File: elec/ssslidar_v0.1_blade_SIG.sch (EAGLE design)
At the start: 30 parts, among them P1 PIN_SMD_0.8X1_RECT, P10 PIN_SMD_0.8X1_RECT, P11 PIN_SMD_1X1_RECT, P12 PIN_SMD_0.8X1_RECT, P13 PIN_SMD_0.8X1_RECT, P14 PIN_SMD_0.8X1_RECT, P15 PIN_SMD_0.8X1_RECT, P16 PIN_SMD_0.8X1_RECT, P17 PIN_SMD_1X1_RECT, P18 PIN_SMD_0.8X1_RECT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

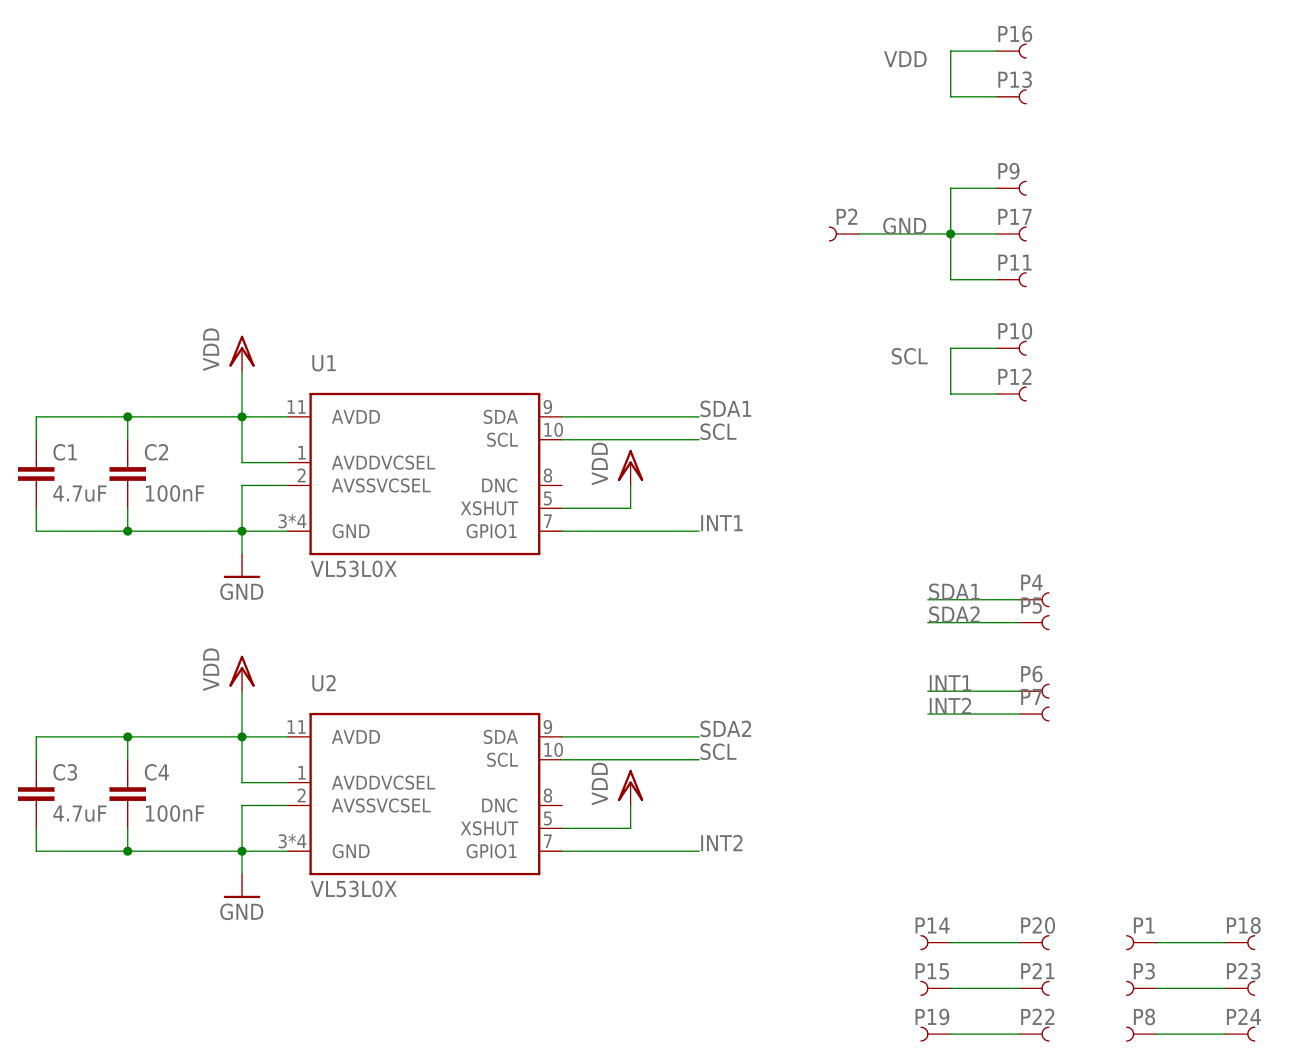
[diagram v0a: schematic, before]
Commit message: Working on main board Made blades longer to avoid too much occlusion from the main PCB (but we will still need to put the whole thing on a mast).
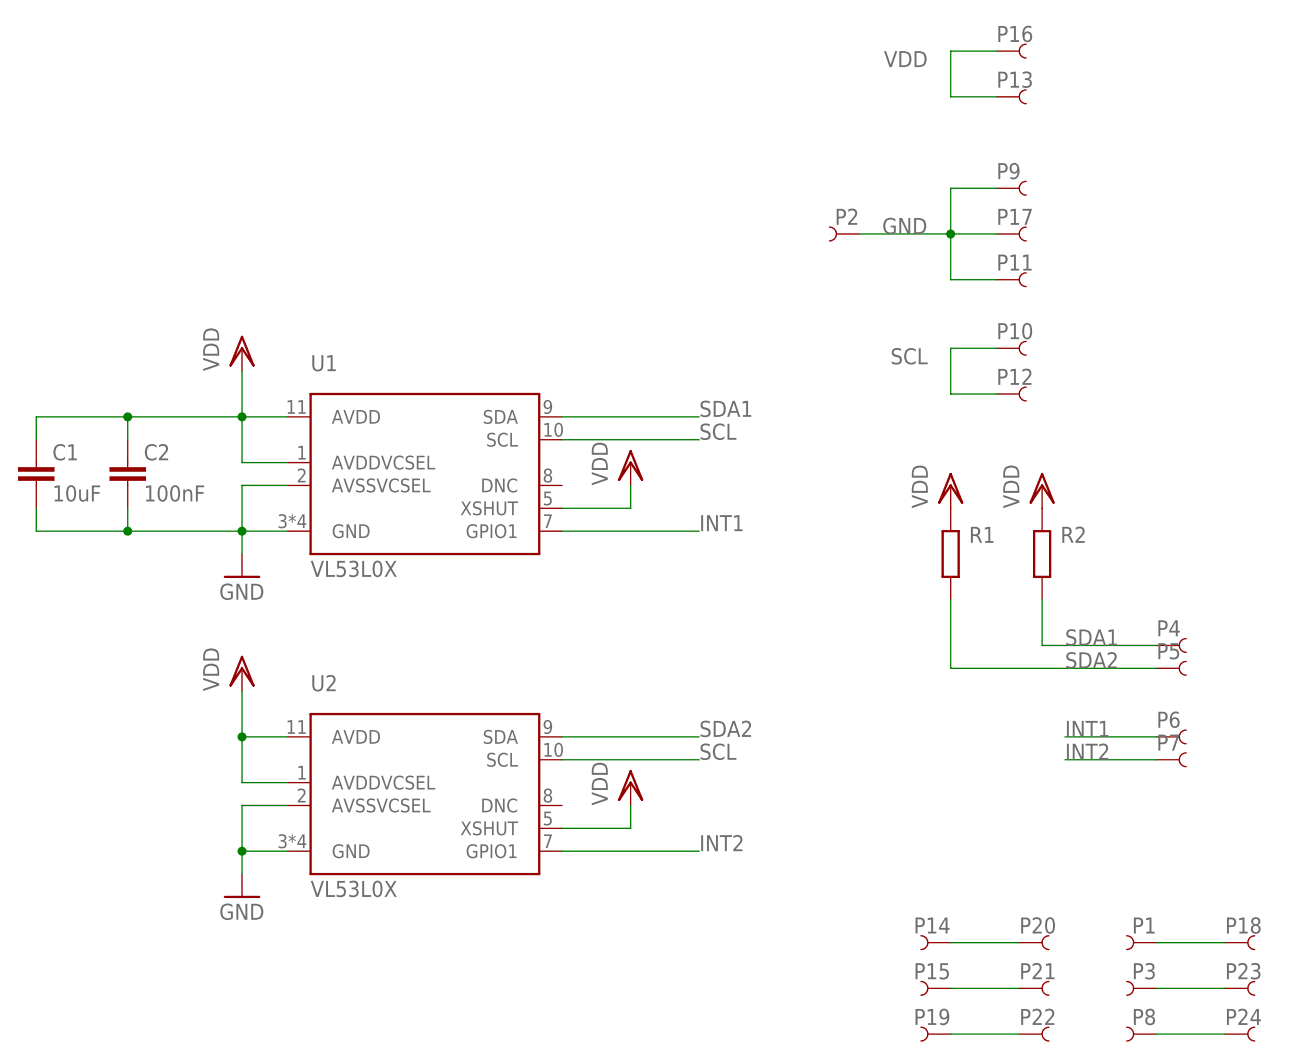
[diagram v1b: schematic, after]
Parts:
- removed C3: 4.7uF, Xevelabs:C0603
- removed C4: 100nF, Xevelabs:C0201
- added R1, R2: (no value), Xevelabs:R0402
- C1: value 4.7uF -> 10uF; device Xevelabs:C0603 -> Xevelabs:C0805
- C2: device Xevelabs:C0201 -> Xevelabs:C0402
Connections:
- net GND: no longer C3.2, C4.2
- net SDA1: now also R2.1
- net SDA2: now also R1.1
- net VDD: now also R1.2, R2.2; no longer C3.1, C4.1
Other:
- moved on the sheet: P4, P5, P6, P7

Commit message: Updated blades (ready for release). Double power rail for sensors.
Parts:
- added C3: 100nF, Xevelabs:C0402
- R1, R2: value (none) -> 2k
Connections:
- net GND: now also C3.2
- net VDD: now also C3.1
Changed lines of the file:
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@@
 <grid distance="0.1" unitdist="inch" unit="inch" style="lines" multiple="1" display="no" altdistance="0.01" altunitdist="inch" altunit="inch"/>
 <layers>
-<layer number="1" name="Top" color="4" fill="1" visible="yes" active="no"/>
-<layer number="2" name="Route2" color="1" fill="3" visible="yes" active="no"/>
-<layer number="3" name="Route3" color="4" fill="3" visible="yes" active="no"/>
-<layer number="14" name="Route14" color="1" fill="6" visible="yes" active="no"/>
-<layer number="15" name="Route15" color="4" fill="6" visible="yes" active="no"/>
-<layer number="16" name="Bottom" color="1" fill="1" visible="yes" active="no"/>
-<layer number="17" name="Pads" color="2" fill="1" visible="yes" active="no"/>
-<layer number="18" name="Vias" color="2" fill="1" visible="yes" active="no"/>
-<layer number="19" name="Unrouted" color="6" fill="1" visible="yes" active="no"/>
-<layer number="20" name="Dimension" color="15" fill="1" visible="yes" active="no"/>
-<layer number="21" name="tPlace" color="7" fill="1" visible="yes" active="no"/>
-<layer number="22" name="bPlace" color="7" fill="1" visible="yes" active="no"/>
-<layer number="23" name="tOrigins" color="15" fill="1" visible="yes" active="no"/>
-<layer number="24" name="bOrigins" color="15" fill="1" visible="yes" active="no"/>
-<layer number="25" name="tNames" color="7" fill="1" visible="yes" active="no"/>
-<layer number="26" name="bNames" color="7" fill="1" visible="yes" active="no"/>
-<layer number="27" name="tValues" color="7" fill="1" visible="yes" active="no"/>
-<layer number="28" name="bValues" color="7" fill="1" visible="yes" active="no"/>
+<layer number="1" name="Top" color="4" fill="1" visible="no" active="no"/>
+<layer number="2" name="Route2" color="1" fill="3" visible="no" active="no"/>
+<layer number="3" name="Route3" color="4" fill="3" visible="no" active="no"/>
+<layer number="14" name="Route14" color="1" fill="6" visible="no" active="no"/>
+<layer number="15" name="Route15" color="4" fill="6" visible="no" active="no"/>
+<layer number="16" name="Bottom" color="1" fill="1" visible="no" active="no"/>
+<layer number="17" name="Pads" color="2" fill="1" visible="no" active="no"/>
+<layer number="18" name="Vias" color="2" fill="1" visible="no" active="no"/>
+<layer number="19" name="Unrouted" color="6" fill="1" visible="no" active="no"/>
+<layer number="20" name="Dimension" color="15" fill="1" visible="no" active="no"/>
+<layer number="21" name="tPlace" color="7" fill="1" visible="no" active="no"/>
+<layer number="22" name="bPlace" color="7" fill="1" visible="no" active="no"/>
+<layer number="23" name="tOrigins" color="15" fill="1" visible="no" active="no"/>
+<layer number="24" name="bOrigins" color="15" fill="1" visible="no" active="no"/>
+<layer number="25" name="tNames" color="7" fill="1" visible="no" active="no"/>
+<layer number="26" name="bNames" color="7" fill="1" visible="no" active="no"/>
+<layer number="27" name="tValues" color="7" fill="1" visible="no" active="no"/>
+<layer number="28" name="bValues" color="7" fill="1" visible="no" active="no"/>
 <layer number="29" name="tStop" color="7" fill="3" visible="no" active="no"/>
 <layer number="30" name="bStop" color="7" fill="6" visible="no" active="no"/>
@@
 <layer number="35" name="tGlue" color="7" fill="4" visible="no" active="no"/>
 <layer number="36" name="bGlue" color="7" fill="5" visible="no" active="no"/>
-<layer number="37" name="tTest" color="7" fill="1" visible="yes" active="no"/>
-<layer number="38" name="bTest" color="7" fill="1" visible="yes" active="no"/>
+<layer number="37" name="tTest" color="7" fill="1" visible="no" active="no"/>
+<layer number="38" name="bTest" color="7" fill="1" visible="no" active="no"/>
 <layer number="39" name="tKeepout" color="4" fill="11" visible="no" active="no"/>
 <layer number="40" name="bKeepout" color="1" fill="11" visible="no" active="no"/>
@@
 <layer number="44" name="Drills" color="7" fill="1" visible="no" active="no"/>
 <layer number="45" name="Holes" color="7" fill="1" visible="no" active="no"/>
-<layer number="46" name="Milling" color="3" fill="1" visible="yes" active="no"/>
-<layer number="47" name="Measures" color="7" fill="1" visible="yes" active="no"/>
-<layer number="48" name="Document" color="7" fill="1" visible="yes" active="no"/>
-<layer number="49" name="Reference" color="7" fill="1" visible="yes" active="no"/>
-<layer number="50" name="dxf" color="7" fill="1" visible="yes" active="no"/>
-<layer number="51" name="tDocu" color="7" fill="1" visible="yes" active="no"/>
-<layer number="52" name="bDocu" color="7" fill="1" visible="yes" active="no"/>
-<layer number="53" name="tGND_GNDA" color="7" fill="9" visible="yes" active="no"/>
-<layer number="54" name="bGND_GNDA" color="1" fill="9" visible="yes" active="no"/>
-<layer number="56" name="wert" color="7" fill="1" visible="yes" active="no"/>
+<layer number="46" name="Milling" color="3" fill="1" visible="no" active="no"/>
+<layer number="47" name="Measures" color="7" fill="1" visible="no" active="no"/>
+<layer number="48" name="Document" color="7" fill="1" visible="no" active="no"/>
+<layer number="49" name="Reference" color="7" fill="1" visible="no" active="no"/>
+<layer number="50" name="dxf" color="7" fill="1" visible="no" active="no"/>
+<layer number="51" name="tDocu" color="7" fill="1" visible="no" active="no"/>
+<layer number="52" name="bDocu" color="7" fill="1" visible="no" active="no"/>
+<layer number="53" name="tGND_GNDA" color="7" fill="9" visible="no" active="no"/>
+<layer number="54" name="bGND_GNDA" color="1" fill="9" visible="no" active="no"/>
+<layer number="56" name="wert" color="7" fill="1" visible="no" active="no"/>
 <layer number="90" name="Modules" color="5" fill="1" visible="yes" active="yes"/>
 <layer number="91" name="Nets" color="2" fill="1" visible="yes" active="yes"/>
@@
 <part name="P23" library="Xevelabs" deviceset="PIN" device="_SMD_0.8X1_RECT" value="PIN_SMD_0.8X1_RECT"/>
 <part name="P24" library="Xevelabs" deviceset="PIN" device="_SMD_0.8X1_RECT" value="PIN_SMD_0.8X1_RECT"/>
-<part name="R1" library="Xevelabs" deviceset="R" device="0402"/>
-<part name="R2" library="Xevelabs" deviceset="R" device="0402"/>
+<part name="R1" library="Xevelabs" deviceset="R" device="0402" value="2k"/>
+<part name="R2" library="Xevelabs" deviceset="R" device="0402" value="2k"/>
 <part name="VDD5" library="supply1" deviceset="VDD" device=""/>
 <part name="VDD6" library="supply1" deviceset="VDD" device=""/>
+<part name="C3" library="Xevelabs" deviceset="C" device="0402" value="100nF"/>
 </parts>
 <sheets>
@@
 <instance part="VDD5" gate="G$1" x="106.68" y="50.8"/>
 <instance part="VDD6" gate="G$1" x="116.84" y="50.8"/>
+<instance part="C3" gate="G$1" x="15.24" y="15.24"/>
 </instances>
 <busses>
@@
 <wire x1="27.94" y1="17.78" x2="27.94" y2="22.86" width="0.1524" layer="91"/>
 <junction x="27.94" y="22.86"/>
+<pinref part="C3" gate="G$1" pin="1"/>
+<wire x1="27.94" y1="22.86" x2="15.24" y2="22.86" width="0.1524" layer="91"/>
+<wire x1="15.24" y1="22.86" x2="15.24" y2="20.32" width="0.1524" layer="91"/>
 </segment>
 <segment>
@@
 <wire x1="27.94" y1="15.24" x2="27.94" y2="10.16" width="0.1524" layer="91"/>
 <junction x="27.94" y="10.16"/>
-</segment>
-<segment>
+<pinref part="C3" gate="G$1" pin="2"/>
+<wire x1="27.94" y1="10.16" x2="15.24" y2="10.16" width="0.1524" layer="91"/>
+<wire x1="15.24" y1="10.16" x2="15.24" y2="12.7" width="0.1524" layer="91"/>
+</segment>
+<segment>
